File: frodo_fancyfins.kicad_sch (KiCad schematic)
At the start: 63 parts, among them J1 Molex MicroFit 2x3, J2 Molex MicroFit 2x3, J3 U.FL, J4 SWD Header, Q1 AO3400A, U1 STM32F072RBTx, U14 AS321KTR-G1, U15 AZ1117-5.0, U16 AZ1117-5.0, U2 MCP2562-E-SN, U3 AZ1117-3.3, Y1 8MHz 12pF

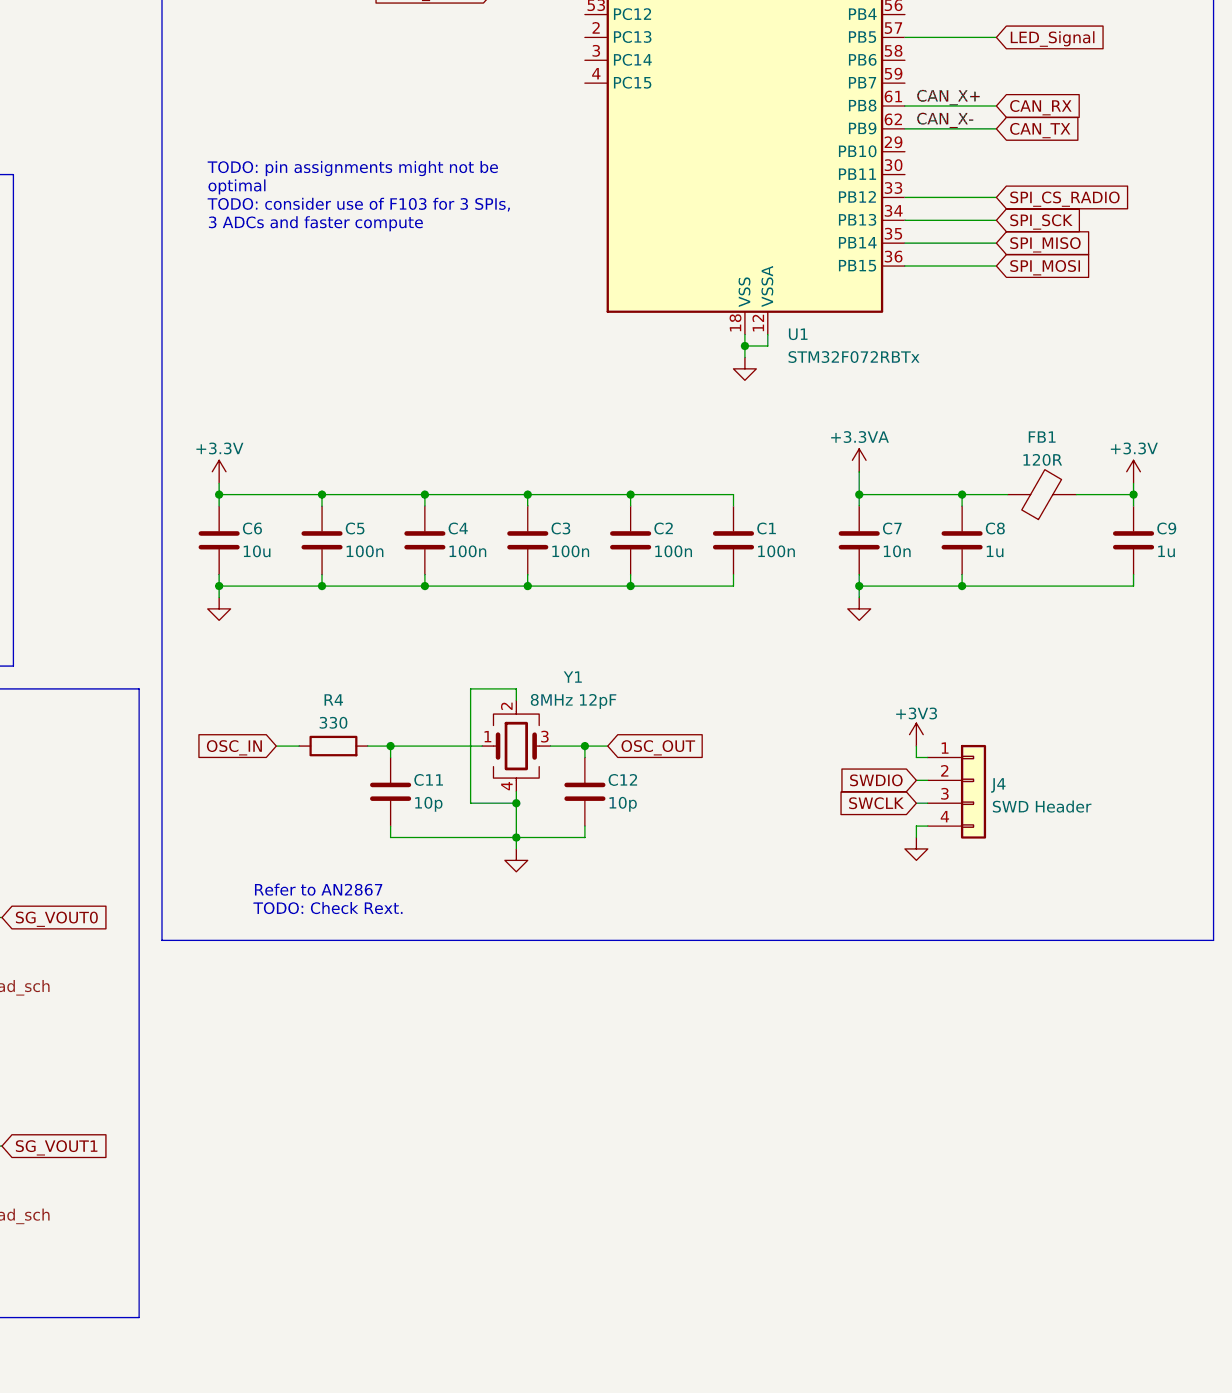
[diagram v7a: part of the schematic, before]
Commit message: Add flash memory schematics
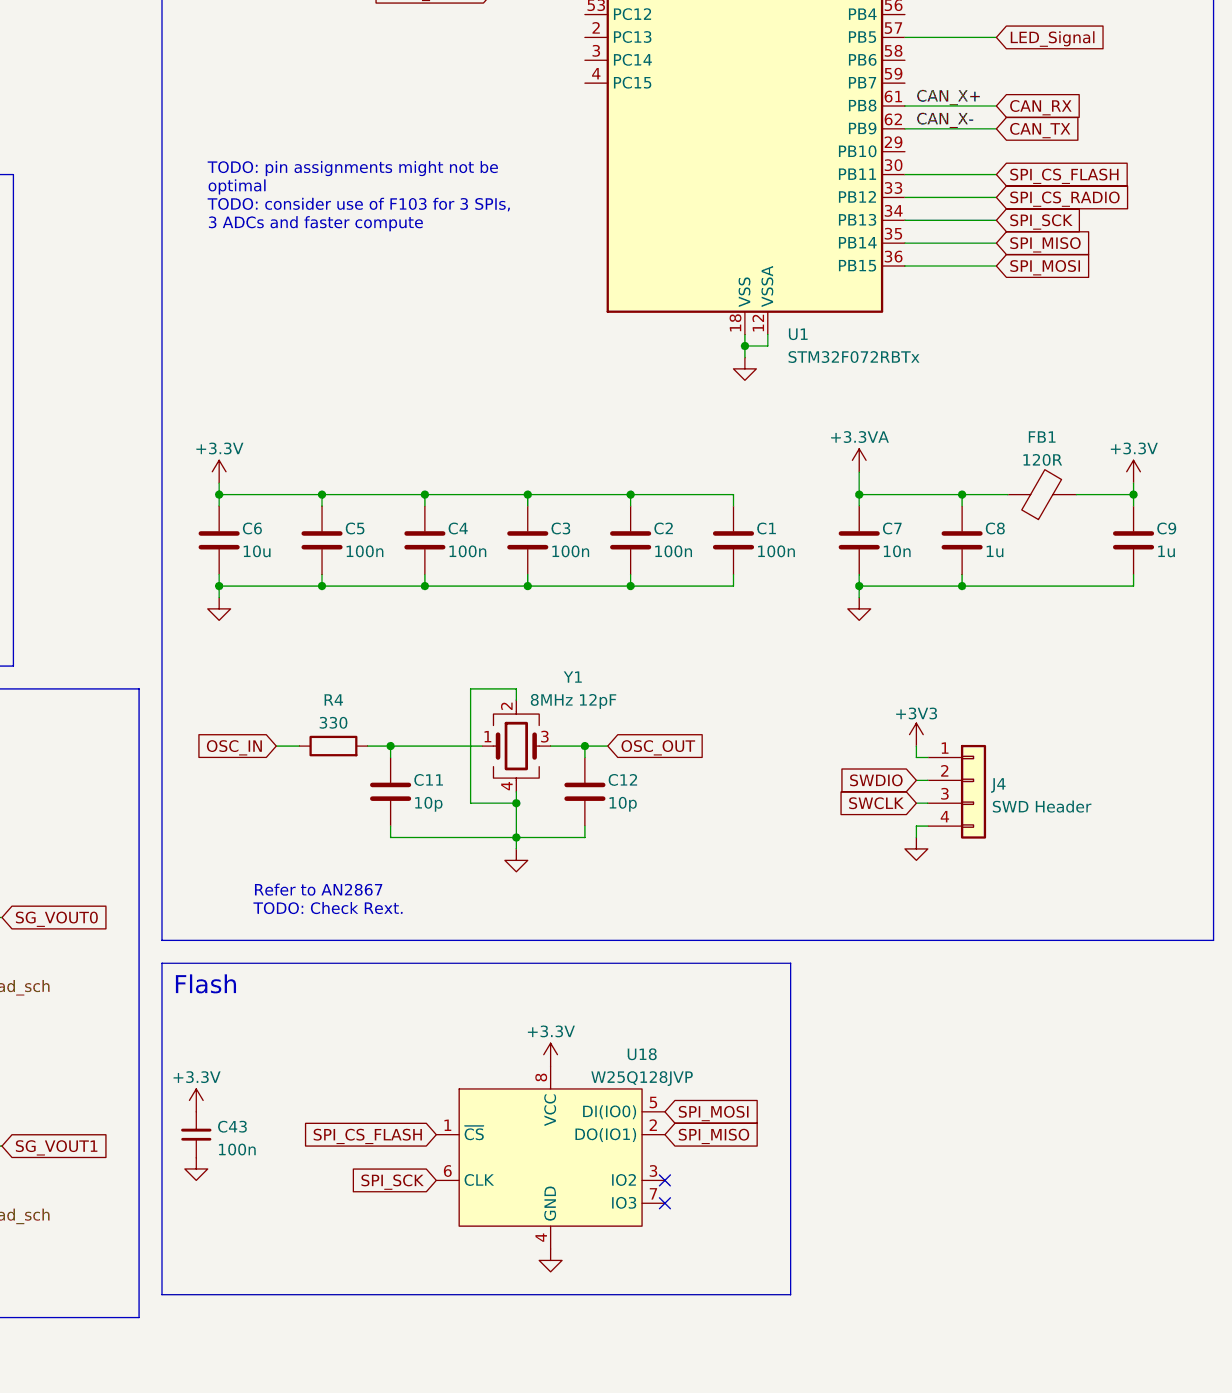
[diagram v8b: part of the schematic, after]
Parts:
- added C43: 100n, Capacitor_SMD:C_0603_1608Metric, symbol Device:C_Small
- added U18: W25Q128JVP, symbol frodo_fancyfins:W25Q128JVP
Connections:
- net +3.3V: now also C43.2, U18.8 (VCC)
- net GND: now also C43.1, U18.4 (GND)
- net SPI_MISO: now also U18.2 (DO(IO1))
- net SPI_MOSI: now also U18.5 (DI(IO0))
- net SPI_SCK: now also U18.6 (CLK)
- net SPI_CS_FLASH: now reaches U1.30 (PB11)
- net SPI_CS_FLASH: now also U18.1 (~{CS})
- no-connect marks 0 -> 2
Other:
- note added: "Flash"
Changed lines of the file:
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@@
   (junction (at 262.89 120.65) (diameter 0) (color 0 0 0 0)
   )
+  (no_connect (at 254 215.9))
+  (no_connect (at 254 213.36))
   (wire (pts (xy 290.83 109.22) (xy 280.67 109.22))
     (stroke (width 0) (type default))
@@
     (stroke (width 0) (type default))
   )
+  (wire (pts (xy 280.67 101.6) (xy 290.83 101.6))
+    (stroke (width 0) (type default))
+  )
   (wire (pts (xy 87.63 219.71) (xy 90.17 219.71))
     (stroke (width 0) (type default))
@@
     (fill (type none))
   )
+  (rectangle (start 198.12 189.23) (end 267.97 226.06)
+    (stroke (width 0) (type default))
+    (fill (type none))
+  )
   (rectangle (start 109.22 158.75) (end 195.58 228.6)
     (stroke (width 0) (type default))
@@
     (effects (font (size 2 2)) (justify left bottom))
   )
+  (text "Flash" (at 199.39 193.04 0)
+    (effects (font (size 2 2)) (justify left bottom))
+  )
   (text "Refer to AN2867\nTODO: Check Rext." (at 208.28 184.15 0)
     (effects (font (size 1.27 1.27)) (justify left bottom))
@@
     )
   )
+  (global_label "SPI_MOSI" (shape input) (at 254 205.74 0) (fields_autoplaced)
+    (effects (font (size 1.27 1.27)) (justify left))
+    (property "Intersheetrefs" "${INTERSHEET_REFS}" (at 265.6333 205.74 0)
+      (effects (font (size 1.27 1.27)) (justify left) hide)
+    )
+  )
+  (global_label "SPI_SCK" (shape input) (at 228.6 213.36 180) (fields_autoplaced)
+    (effects (font (size 1.27 1.27)) (justify right))
+    (property "Intersheetrefs" "${INTERSHEET_REFS}" (at 217.8134 213.36 0)
+      (effects (font (size 1.27 1.27)) (justify right) hide)
+    )
+  )
   (global_label "RST_RADIO" (shape input) (at 31.75 180.34 180) (fields_autoplaced)
     (effects (font (size 1.27 1.27)) (justify right))
@@
     )
   )
+  (global_label "SPI_MISO" (shape input) (at 254 208.28 0) (fields_autoplaced)
+    (effects (font (size 1.27 1.27)) (justify left))
+    (property "Intersheetrefs" "${INTERSHEET_REFS}" (at 265.6333 208.28 0)
+      (effects (font (size 1.27 1.27)) (justify left) hide)
+    )
+  )
+  (global_label "SPI_CS_FLASH" (shape input) (at 290.83 101.6 0) (fields_autoplaced)
+    (effects (font (size 1.27 1.27)) (justify left))
+    (property "Intersheetrefs" "${INTERSHEET_REFS}" (at 307.0595 101.6 0)
+      (effects (font (size 1.27 1.27)) (justify left) hide)
+    )
+  )
   (global_label "SG_EN" (shape input) (at 234.95 53.34 180) (fields_autoplaced)
     (effects (font (size 1.27 1.27)) (justify right))
@@
     )
   )
+  (global_label "SPI_CS_FLASH" (shape input) (at 228.6 208.28 180) (fields_autoplaced)
+    (effects (font (size 1.27 1.27)) (justify right))
+    (property "Intersheetrefs" "${INTERSHEET_REFS}" (at 212.3705 208.28 0)
+      (effects (font (size 1.27 1.27)) (justify right) hide)
+    )
+  )
   (global_label "SPI_CS_RADIO" (shape input) (at 31.75 184.15 180) (fields_autoplaced)
     (effects (font (size 1.27 1.27)) (justify right))
@@
     )
   )
+  (symbol (lib_id "frodo_fancyfins:W25Q128JVP") (at 241.3 210.82 0) (unit 1)
+    (in_bom yes) (on_board yes) (dnp no) (fields_autoplaced)
+    (property "Reference" "U18" (at 251.46 199.39 0) (do_not_autoplace)
+      (effects (font (size 1.27 1.27)))
+    )
+    (property "Value" "W25Q128JVP" (at 251.46 201.93 0) (do_not_autoplace)
+      (effects (font (size 1.27 1.27)))
+    )
+    (property "Footprint" "" (at 241.3 210.82 0)
+      (effects (font (size 1.27 1.27)) hide)
+    )
+    (property "Datasheet" "" (at 241.3 210.82 0)
+      (effects (font (size 1.27 1.27)) hide)
+    )
+    (pin "7")
+    (pin "6")
+    (pin "4")
+    (pin "1")
+    (pin "5")
+    (pin "2")
+    (pin "3")
+    (pin "8")
+    (instances
+      (project "frodo_fancyfins"
+        (path "/6b822b14-450b-45c3-a34b-8e18c5811754"
+          (reference "U18") (unit 1)
+        )
+      )
+    )
+  )
   (symbol (lib_id "Regulator_Linear:AZ1117-5.0") (at 93.98 29.21 0) (unit 1)
     (in_bom yes) (on_board yes) (dnp no) (fields_autoplaced)
@@
     )
   )
+  (symbol (lib_id "Device:C_Small") (at 201.93 208.28 180) (unit 1)
+    (in_bom yes) (on_board yes) (dnp no) (fields_autoplaced)
+    (property "Reference" "C43" (at 204.2541 207.4389 0)
+      (effects (font (size 1.27 1.27)) (justify right))
+    )
+    (property "Value" "100n" (at 204.2541 209.9758 0)
+      (effects (font (size 1.27 1.27)) (justify right))
+    )
+    (property "Footprint" "Capacitor_SMD:C_0603_1608Metric" (at 201.93 208.28 0)
+      (effects (font (size 1.27 1.27)) hide)
+    )
+    (property "Datasheet" "~" (at 201.93 208.28 0)
+      (effects (font (size 1.27 1.27)) hide)
+    )
+    (property "LCSC#" "C1591" (at 201.93 208.28 0)
+      (effects (font (size 1.27 1.27)) hide)
+    )
+    (property "Manufacturer" "Samsung Electro-Mechanics" (at 201.93 208.28 0)
+      (effects (font (size 1.27 1.27)) hide)
+    )
+    (property "Part#" "CL10B104KB8NNNC" (at 201.93 208.28 0)
+      (effects (font (size 1.27 1.27)) hide)
+    )
+    (pin "1")
+    (pin "2")
+    (instances
+      (project "frodo_fancyfins"
+        (path "/6b822b14-450b-45c3-a34b-8e18c5811754"
+          (reference "C43") (unit 1)
+        )
+      )
+      (project "euroc_fc"
+        (path "/e63e39d7-6ac0-4ffd-8aa3-1841a4541b55"
+          (reference "C38") (unit 1)
+        )
+      )
+    )
+  )
+  (symbol (lib_id "power:+3.3V") (at 241.3 200.66 0) (unit 1)
+    (in_bom yes) (on_board yes) (dnp no)
+    (property "Reference" "#PWR084" (at 241.3 204.47 0)
+      (effects (font (size 1.27 1.27)) hide)
+    )
+    (property "Value" "+3.3V" (at 241.3 196.85 0)
+      (effects (font (size 1.27 1.27)))
+    )
+    (property "Footprint" "" (at 241.3 200.66 0)
+      (effects (font (size 1.27 1.27)) hide)
+    )
+    (property "Datasheet" "" (at 241.3 200.66 0)
+      (effects (font (size 1.27 1.27)) hide)
+    )
+    (pin "1")
+    (instances
+      (project "frodo_fancyfins"
+        (path "/6b822b14-450b-45c3-a34b-8e18c5811754"
+          (reference "#PWR084") (unit 1)
+        )
+      )
+    )
+  )
   (symbol (lib_id "Device:C") (at 245.11 170.18 0) (unit 1)
     (in_bom yes) (on_board yes) (dnp no)
@@
     )
   )
+  (symbol (lib_id "power:GND") (at 201.93 210.82 0) (unit 1)
+    (in_bom yes) (on_board yes) (dnp no) (fields_autoplaced)
+    (property "Reference" "#PWR085" (at 201.93 217.17 0)
+      (effects (font (size 1.27 1.27)) hide)
+    )
+    (property "Value" "GND" (at 201.93 215.2634 0)
+      (effects (font (size 1.27 1.27)) hide)
+    )
+    (property "Footprint" "" (at 201.93 210.82 0)
+      (effects (font (size 1.27 1.27)) hide)
+    )
+    (property "Datasheet" "" (at 201.93 210.82 0)
+      (effects (font (size 1.27 1.27)) hide)
+    )
+    (pin "1")
+    (instances
+      (project "frodo_fancyfins"
+        (path "/6b822b14-450b-45c3-a34b-8e18c5811754"
+          (reference "#PWR085") (unit 1)
+        )
+      )
+      (project "euroc_fc"
+        (path "/e63e39d7-6ac0-4ffd-8aa3-1841a4541b55"
+          (reference "#PWR019") (unit 1)
+        )
+      )
+    )
+  )
   (symbol (lib_id "power:VD") (at 54.61 125.73 0) (unit 1)
     (in_bom yes) (on_board yes) (dnp no)
@@
     )
   )
+  (symbol (lib_id "power:+3.3V") (at 201.93 205.74 0) (unit 1)
+    (in_bom yes) (on_board yes) (dnp no)
+    (property "Reference" "#PWR086" (at 201.93 209.55 0)
+      (effects (font (size 1.27 1.27)) hide)
+    )
+    (property "Value" "+3.3V" (at 201.93 201.93 0)
+      (effects (font (size 1.27 1.27)))
+    )
+    (property "Footprint" "" (at 201.93 205.74 0)
+      (effects (font (size 1.27 1.27)) hide)
+    )
+    (property "Datasheet" "" (at 201.93 205.74 0)
+      (effects (font (size 1.27 1.27)) hide)
+    )
+    (pin "1")
+    (instances
+      (project "frodo_fancyfins"
+        (path "/6b822b14-450b-45c3-a34b-8e18c5811754"
+          (reference "#PWR086") (unit 1)
+        )
+      )
+    )
+  )
   (symbol (lib_id "power:+VSW") (at 43.18 24.13 270) (mirror x) (unit 1)
     (in_bom yes) (on_board yes) (dnp no) (fields_autoplaced)
@@
         )
       )
+    )
+  )
+  (symbol (lib_id "power:GND") (at 241.3 220.98 0) (unit 1)
+    (in_bom yes) (on_board yes) (dnp no) (fields_autoplaced)
+    (property "Reference" "#PWR087" (at 241.3 227.33 0)
+      (effects (font (size 1.27 1.27)) hide)
+    )
+    (property "Value" "GND" (at 241.3 225.4234 0)
+      (effects (font (size 1.27 1.27)) hide)
+    )
+    (property "Footprint" "" (at 241.3 220.98 0)
+      (effects (font (size 1.27 1.27)) hide)
+    )
+    (property "Datasheet" "" (at 241.3 220.98 0)
+      (effects (font (size 1.27 1.27)) hide)
+    )
+    (pin "1")
+    (instances
+      (project "frodo_fancyfins"
+        (path "/6b822b14-450b-45c3-a34b-8e18c5811754"
+          (reference "#PWR087") (unit 1)
+        )
+      )
+      (project "euroc_fc"
+        (path "/e63e39d7-6ac0-4ffd-8aa3-1841a4541b55"
+          (reference "#PWR019") (unit 1)
+        )
+      )
